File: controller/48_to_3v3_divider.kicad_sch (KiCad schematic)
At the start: 5 parts

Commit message: Controller - Try to simplify
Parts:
- renumbered C26 to C23, R76 to R33, R77 to R34, R78 to R35, R79 to R36
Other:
- removed sheet 3v3_clamp11
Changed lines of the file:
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@@
-	)
-	(junction
-		(at 44.45 30.48)
-		(diameter 0)
-		(color 0 0 0 0)
 	)
 	(junction
@@
 	(wire
 		(pts
-			(xy 44.45 26.67) (xy 44.45 30.48)
-		)
-		(stroke
-			(width 0)
-			(type default)
-		)
-	)
-	(wire
-		(pts
-			(xy 44.45 30.48) (xy 46.99 30.48)
-		)
-		(stroke
-			(width 0)
-			(type default)
-		)
-	)
-	(wire
-		(pts
-			(xy 46.99 26.67) (xy 44.45 26.67)
-		)
-		(stroke
-			(width 0)
-			(type default)
-		)
-	)
-	(wire
-		(pts
 			(xy 35.56 30.48) (xy 38.1 30.48)
 		)
@@
 	(hierarchical_label "OUT"
 		(shape output)
-		(at 46.99 26.67 0)
+		(at 44.45 30.48 0)
 		(fields_autoplaced yes)
 		(effects
@@
 		(on_board yes)
 		(dnp no)
-		(property "Reference" "R77"
+		(property "Reference" "R34"
 			(at 31.242 22.352 0)
 			(effects
@@
 		(on_board yes)
 		(dnp no)
-		(property "Reference" "R79"
+		(property "Reference" "R36"
 			(at 35.052 22.352 0)
 			(effects
@@
 		(on_board yes)
 		(dnp no)
-		(property "Reference" "R78"
+		(property "Reference" "R35"
 			(at 32.258 28.702 0)
 			(effects
@@
 		(dnp no)
 		(fields_autoplaced yes)
-		(property "Reference" "#PWR090"
+		(property "Reference" "#PWR053"
 			(at 31.75 41.91 0)
 			(effects
@@
 		(on_board yes)
 		(dnp no)
-		(property "Reference" "R76"
+		(property "Reference" "R33"
 			(at 28.448 23.622 0)
 			(effects
@@
 		(on_board yes)
 		(dnp no)
-		(property "Reference" "C26"
+		(property "Reference" "C23"
 			(at 36.068 28.194 0)
 			(effects
@@
 				)
 			)
-		)
-	)
-	(sheet
-		(at 46.99 27.94)
-		(size 12.7 3.81)
-		(stroke
-			(width 0.1524)
-			(type solid)
-		)
-		(fill
-			(color 0 0 0 0.0000)
-		)
-		(property "Sheetname" "3v3_clamp11"
-			(at 46.99 29.718 0)
-			(effects
-				(font
-					(size 1.27 1.27)
-				)
-				(justify left bottom)
-			)
-		)
-		(property "Sheetfile" "mcu_clamp.kicad_sch"
-			(at 46.99 32.3346 0)
-			(effects
-				(font
-					(size 1.27 1.27)
-				)
-				(justify left top)
-				(hide yes)
-			)
-		)
-		(pin "S" passive
-			(at 46.99 30.48 180)
-			(effects
-				(font
-					(size 1.27 1.27)
-				)
-				(justify left)
-			)
-		)
-		(instances
-			(project "controller"
-				(path "/5b092a03-7e3e-4df1-ad91-2ac0e362f857/3a11ce7c-7e29-4758-a12a-8535ab4c73af"
-					(page "2")
-				)
-				(path "/5b092a03-7e3e-4df1-ad91-2ac0e362f857/8b76543b-a49c-413b-a98c-7f3e228c6216"
-					(page "4")
-				)
-				(path "/5b092a03-7e3e-4df1-ad91-2ac0e362f857/a5d84eb1-8829-4f32-a763-e01f5977372c"
-					(page "13")
-				)
-				(path "/5b092a03-7e3e-4df1-ad91-2ac0e362f857/2f911ebd-6dc8-4496-8afb-4a9ec6bafab7"
-					(page "15")
-				)
-				(path "/5b092a03-7e3e-4df1-ad91-2ac0e362f857/dfe157ff-eae8-44d0-adc3-b7fe75c1e740"
-					(page "17")
-				)
-				(path "/5b092a03-7e3e-4df1-ad91-2ac0e362f857/e3d09b0d-badf-46a0-b7fb-f25da99c9c12"
-					(page "19")
-				)
-			)

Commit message: Controller - More work mainly on layout
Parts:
- removed R33, R34, R36: R_Small, Resistor_SMD:R_0805_2012Metric, symbol Device:R_Small
- C23: footprint Capacitor_SMD:C_0402_1005Metric -> Capacitor_SMD:C_0402_1005Metric_Pad0.74x0.62mm_HandSolder
- R35: footprint Resistor_SMD:R_0603_1608Metric -> Resistor_SMD:R_0402_1005Metric_Pad0.72x0.64mm_HandSolder
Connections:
- net OUT is gone; now on net IN: C23.1, R35.1

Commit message: Controller - some more changes
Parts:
- C23: value 100nF -> 10nF
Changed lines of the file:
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@@
 			)
 		)
-		(property "Value" "100nF"
+		(property "Value" "10nF"
 			(at 35.052 38.354 0)
 			(effects

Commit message: Controller - More routing
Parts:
- C23: footprint Capacitor_SMD:C_0402_1005Metric_Pad0.74x0.62mm_HandSolder -> Capacitor_SMD:C_0402_1005Metric
- R35: footprint Resistor_SMD:R_0402_1005Metric_Pad0.72x0.64mm_HandSolder -> Resistor_SMD:R_0402_1005Metric
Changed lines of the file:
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@@
 			)
 		)
-		(property "Footprint" "Resistor_SMD:R_0402_1005Metric_Pad0.72x0.64mm_HandSolder"
+		(property "Footprint" "Resistor_SMD:R_0402_1005Metric"
 			(at 31.75 33.02 0)
 			(effects
@@
 			)
 		)
-		(property "Footprint" "Capacitor_SMD:C_0402_1005Metric_Pad0.74x0.62mm_HandSolder"
+		(property "Footprint" "Capacitor_SMD:C_0402_1005Metric"
 			(at 38.1 33.02 0)
 			(effects

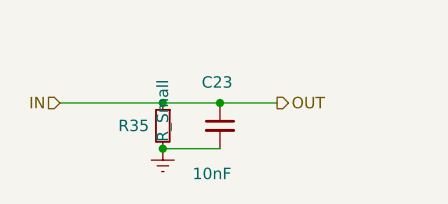
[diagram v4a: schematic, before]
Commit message: controller - Update BOM - WIP
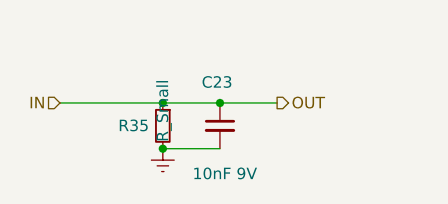
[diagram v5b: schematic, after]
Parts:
- C23: value 10nF -> 10nF 9V
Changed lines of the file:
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@@
+			)
+		)
+		(property "MFR" ""
+			(at 31.75 33.02 0)
+			(effects
+				(font
+					(size 1.27 1.27)
+				)
+				(hide yes)
+			)
+		)
+		(property "part-num" ""
+			(at 31.75 33.02 0)
+			(effects
+				(font
+					(size 1.27 1.27)
+				)
+				(hide yes)
 			)
 		)
@@
 			)
 		)
-		(property "Value" "10nF"
+		(property "Value" "10nF 9V"
 			(at 35.052 38.354 0)
 			(effects
@@
 			(at 38.1 33.02 0)
 			(effects
+				(font
+					(size 1.27 1.27)
+				)
+				(hide yes)
+			)
+		)
+		(property "MFR" ""
+			(at 38.1 33.02 0)
+			(effects
+				(font
+					(size 1.27 1.27)
+				)
+				(hide yes)
+			)
+		)
+		(property "part-num" ""
+			(at 38.1 33.02 0)
+			(effects

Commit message: controller - Update BOM
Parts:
- C23: value 10nF 9V -> 1nF 9V; ARTIKELKOD (none) -> 065-00227
- R35: value R_Small -> 3k3; ARTIKELKOD (none) -> 035-00261 (0603)
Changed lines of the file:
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@@
 			)
 		)
-		(property "Value" "R_Small"
+		(property "Value" "3k3"
 			(at 31.75 34.798 90)
 			(effects
@@
 		)
 		(property "part-num" ""
+			(at 31.75 33.02 0)
+			(effects
+				(font
+					(size 1.27 1.27)
+				)
+				(hide yes)
+			)
+		)
+		(property "ARTIKELKOD" "035-00261 (0603)"
 			(at 31.75 33.02 0)
 			(effects
@@
 			)
 		)
-		(property "Value" "10nF 9V"
+		(property "Value" "1nF 9V"
 			(at 35.052 38.354 0)
 			(effects
@@
 			(at 38.1 33.02 0)
 			(effects
+				(font
+					(size 1.27 1.27)
+				)
+				(hide yes)
+			)
+		)
+		(property "ARTIKELKOD" "065-00227"
+			(at 38.1 33.02 0)
+			(effects
